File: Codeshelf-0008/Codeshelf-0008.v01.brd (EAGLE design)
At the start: 140.5 x 104 mm, 41 parts, among them IC1 74AHC1G04DCK, IC2 74AHC1G04DCK, IC3 74AHC1G04DCK, IC4 74AHC1G08DCK, IC5 74AHC1G08DCK, IC6 74AHC1G08DCK, J1 M05X2PTH, J2 POWER_JACKPTH, J3 M08X2, J4 M08X2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

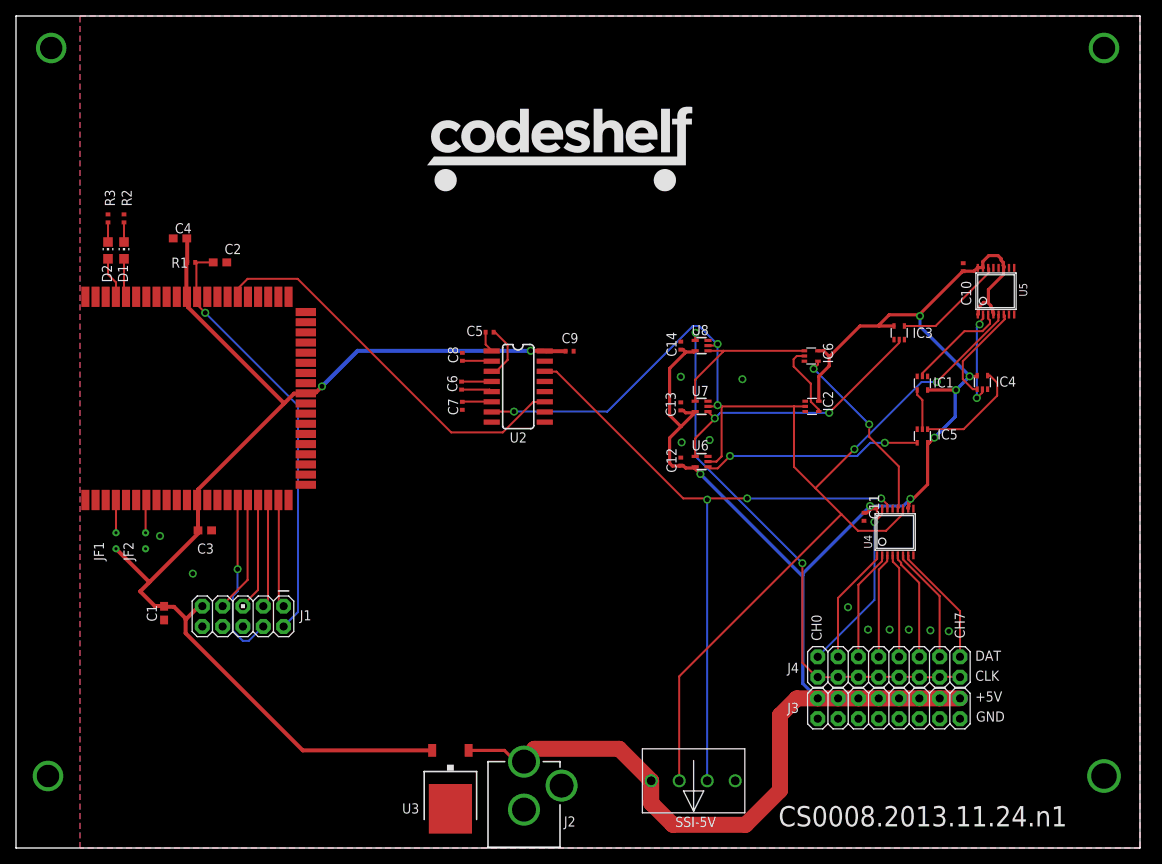
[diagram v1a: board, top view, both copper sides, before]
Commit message: New position controller design
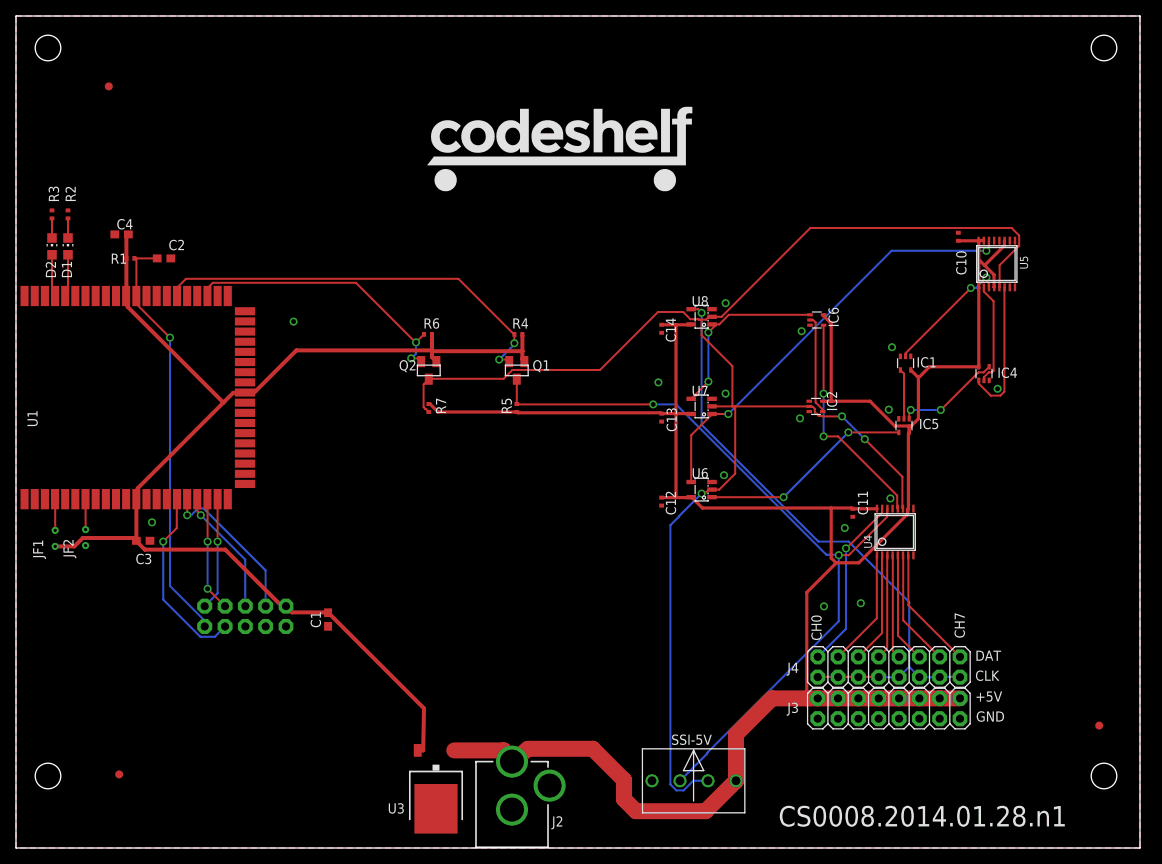
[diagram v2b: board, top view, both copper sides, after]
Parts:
- removed C5, C6, C7, C8, C9: .1uF, GW-devices:C0402
- removed IC3: 74AHC1G04DCK, 74xx-little-us:SC70-5
- removed U2: MAX232SOIC16, SparkFun:SO016
- added Q1, Q2: MOSFET-NCHANNELBSS138, SparkFun-DiscreteSemi:SOT23
- added R4, R5, R6, R7: 10K, GW-devices:RF-R0402
- added U$2, U$3, U$4: FIDUCIAL, adafruit:FIDUCIAL_1MM
- U6, U7, U8: value D-FLIP-FLOP-74LV1G79 -> D-FLIP-FLOP-74LV1G79DBVR; device GW-devices:SOT353 -> GW-devices:SOT23-5
- moved C1 20.5 mm to (39.0, 28.6)
- moved C3 7.81 mm to (15.9, 38.4)
- moved R1 7.62 mm to (14.3, 73.7)
- moved JF1 7.61 mm to (4.90, 38.7)
- moved U1 7.60 mm to (29.9, 56.3)
- moved JF2 7.51 mm to (8.70, 38.8)
- moved C4 7.32 mm to (13.2, 76.7)
- moved C2 7.02 mm to (18.5, 73.7)
- moved D1 7.02 mm to (6.50, 75.2)
- moved D2 7.02 mm to (4.50, 75.2)
- moved R2 7.02 mm to (6.50, 79.2)
- moved R3 7.02 mm to (4.50, 79.2)
- moved C12 5.55 mm to (80.7, 43.3), turned to 90 degrees
- moved IC6 4.55 mm to (100.1, 66.0)
- moved C10 3.85 mm to (117.8, 76.4)
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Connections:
- removed net C1: C5.1, U2.1
- removed net C2: C6.1, U2.4
- removed net N$11: C6.2, U2.5
- removed net N$12: C7.1, U2.6
- removed net N$15: C8.1, U2.2
- removed net N$32: IC3.4, U5.14
- removed net N$8: C5.2, U2.3
- net +3V3: now also Q1.1, Q2.1, R4.1, R6.1; no longer C9.1, U2.16
- net +5V: now also R5.1, R7.1; no longer IC3.5
- net GND: no longer C7.2, C8.2, C9.2, IC3.3, U2.15
- net N$25: now also U5.14; no longer IC3.2
- net SSI-CLK-3V3: now also Q2.2, R6.2
- net SSI-CLK-5V: now also Q2.3, R7.2; no longer U2.7
- net SSI-TX-3V3: now also Q1.2, R4.2; no longer U2.11
- net SSI-TX-5V: now also Q1.3, R5.2; no longer U2.14
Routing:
- net SSI-CLK-3V3: track 0.00 -> 35.5 mm, vias 0 -> 2
- net +5V: track 244.0 -> 279.3 mm, vias 7 -> 0
- net SSI-CLK-5V: track 163.1 -> 196.2 mm, vias 5 -> 3
- net N$25: track 34.3 -> 53.7 mm
- net N$32: track 14.0 -> 0.00 mm
- net SSI-TX-5V: track 85.6 -> 96.7 mm, vias 3 -> 2
- net SSI-CLK: track 68.4 -> 77.8 mm, vias 2 -> 1
- net +3V3: track 149.2 -> 156.5 mm, vias 2 -> 0
- net N$8: track 6.88 -> 0.00 mm
- net TDO: track 14.6 -> 19.8 mm, vias 0 -> 1
- net N$31: track 12.6 -> 17.5 mm
- net N$33: track 23.1 -> 27.9 mm
- net N$26: track 19.8 -> 23.7 mm, vias 0 -> 2
- net N$11: track 3.87 -> 0.00 mm
- net C2: track 3.77 -> 0.00 mm
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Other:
- board text added: "CS0008.2014.01.28.n1"
- board text removed: "CS0008.2013.11.24.n1"
